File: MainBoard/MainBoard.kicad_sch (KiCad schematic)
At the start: 65 parts, among them J1 1761681-3, J2 Non-Inverting Input, J3 Inverting Input, J4 Output, J5 InvertedOutput, J6 Inverting Input, J7 Non-Inverting Input, J8 Output, J9 InvertedOutput, Q16 BC557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

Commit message: plot at tip output
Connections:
- net Comparator-1-InvertedOutput: now also D25.2 (A), D26.1 (K), Q16.3 (E), R1.2, R12.1; no longer J5.2, J5.3, R12.2
- net Comparator-2-InvertedOutput: now also D7.2 (A), D8.1 (K), Q32.3 (E), R13.1, R5.2; no longer J9.2, J9.3, R13.2
- net /Comparator-1/Output: now also D23.2 (A), D24.1 (K), D29.2 (A), Q16.2 (B), R11.1, R2.2; no longer J4.2, J4.3, R11.2
- net /Comparator-2/Output: now also D30.2 (A), Q32.2 (B), R14.1, R3.2; no longer J8.3, R14.2
- new net InvertedOutput-1: J5.2, J5.3, R12.2
- new net InvertedOutput-2: J9.2, J9.3, R13.2
- new net Output-1: J4.2, J4.3, R11.2
- new net Output-2: J8.3, R14.2
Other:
- note added: ".options method=gear gmin=1e-9 cshunt=1e-12 .options reltol=1e-2 abstol=1e-9 vntol=1e-6 .options itl1=300 itl4=300 .options maxstep=100p temp=60 .tran 100u 1000ms .control run plot V("/root/Comparator-1/NonInvertingInput") + V("/root/Comparator-1/InvertingInput") V("/root/Comparator-2/NonInvertingInput") + V("/Output-1") title "Comparator1 Output" plot V("/root/Comparator-1/NonInvertingInput") + 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"
- note removed: ".options method=gear gmin=1e-9 cshunt=1e-12 .options reltol=1e-2 abstol=1e-9 vntol=1e-6 .options itl1=300 itl4=300 .options maxstep=100p temp=60 .tran 100u 1000ms .control run plot V("/root/Comparator-1/NonInvertingInput") + V("/root/Comparator-1/InvertingInput") V("/root/Comparator-2/NonInvertingInput") + V("/root/Comparator-1/Output") title "Comparator1 Output" plot V("/root/Comparator-1/NonInv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"
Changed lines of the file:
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@@
 		)
 	)
-	(text ".options method=gear gmin=1e-9 cshunt=1e-12 \n.options reltol=1e-2 abstol=1e-9 vntol=1e-6 \n.options itl1=300 itl4=300 \n.options maxstep=100p temp=60\n.tran 100u 1000ms\n.control\nrun\nplot V(\"/root/Comparator-1/NonInvertingInput\") \n     + V(\"/root/Comparator-1/InvertingInput\") V(\"/root/Comparator-2/NonInvertingInput\") \n     + V(\"/root/Comparator-1/Output\") title \"Comparator1 Output\" \nplot V(\"/root/Comparator-1/NonInvertingInput\")\n     + V(\"/root/Comparator-1/InvertingInput\") V(\"/root/Comparator-2/NonInvertingInput\") \n     + V(\"/Comparator-1-InvertedOutput\") title \"Comparator1 Inverted-Output\"\nplot V(\"/root/Comparator-2/InvertingInput\") \n     + V(\"/root/Comparator-1/InvertingInput\") V(\"/root/Comparator-2/NonInvertingInput\")   \n     + V(\"/root/Comparator-2/Output\") title \"Comparator2 Output\" \nplot V(\"/root/Comparator-2/InvertingInput\")\n     + V(\"/root/Comparator-1/InvertingInput\") V(\"/root/Comparator-2/NonInvertingInput\") \n     + V(\"/Comparator-2-InvertedOutput\") title \"Comparator2 Inverted-Output\"\n.endc"
+	(text ".options method=gear gmin=1e-9 cshunt=1e-12 \n.options reltol=1e-2 abstol=1e-9 vntol=1e-6 \n.options itl1=300 itl4=300 \n.options maxstep=100p temp=60\n.tran 100u 1000ms\n.control\nrun\nplot V(\"/root/Comparator-1/NonInvertingInput\") \n     + V(\"/root/Comparator-1/InvertingInput\") V(\"/root/Comparator-2/NonInvertingInput\") \n     + V(\"/Output-1\") title \"Comparator1 Output\" \nplot V(\"/root/Comparator-1/NonInvertingInput\")\n     + V(\"/root/Comparator-1/InvertingInput\") V(\"/root/Comparator-2/NonInvertingInput\") \n     + V(\"/InvertedOutput-1\") title \"Comparator1 Inverted-Output\"\nplot V(\"/root/Comparator-2/InvertingInput\") \n     + V(\"/root/Comparator-1/InvertingInput\") V(\"/root/Comparator-2/NonInvertingInput\")   \n     + V(\"/Output-2\") title \"Comparator2 Output\" \nplot V(\"/root/Comparator-2/InvertingInput\")\n     + V(\"/root/Comparator-1/InvertingInput\") V(\"/root/Comparator-2/NonInvertingInput\") \n     + V(\"/InvertedOutput-2\") title \"Comparator2 Inverted-Output\"\n.endc"
 		(exclude_from_sim no)
 		(at 170.688 147.066 0)
@@
 	)
 	(junction
+		(at 250.19 88.9)
+		(diameter 0)
+		(color 0 0 0 0)
+	)
+	(junction
 		(at 49.53 29.21)
 		(diameter 0)
@@
 	)
 	(junction
-		(at 250.19 88.9)
-		(diameter 0)
-		(color 0 0 0 0)
-	)
-	(junction
 		(at 62.23 116.84)
 		(diameter 0)
@@
 	(wire
 		(pts
-			(xy 254 57.15) (xy 254 53.34)
-		)
-		(stroke
-			(width 0)
-			(type default)
-		)
-	)
-	(wire
-		(pts
-			(xy 250.19 33.02) (xy 250.19 29.21)
+			(xy 250.19 33.02) (xy 251.46 33.02)
+		)
+		(stroke
+			(width 0)
+			(type default)
+		)
+	)
+	(wire
+		(pts
+			(xy 254 113.03) (xy 254 116.84)
+		)
+		(stroke
+			(width 0)
+			(type default)
+		)
+	)
+	(wire
+		(pts
+			(xy 222.25 53.34) (xy 226.06 53.34)
+		)
+		(stroke
+			(width 0)
+			(type default)
+		)
+	)
+	(wire
+		(pts
+			(xy 213.36 29.21) (xy 217.17 29.21)
 		)
 		(stroke
@@
 	(wire
 		(pts
+			(xy 254 53.34) (xy 254 57.15)
+		)
+		(stroke
+			(width 0)
+			(type default)
+		)
+	)
+	(wire
+		(pts
 			(xy 96.52 173.99) (xy 96.52 175.26)
 		)
@@
 	(wire
 		(pts
-			(xy 254 116.84) (xy 254 113.03)
+			(xy 254 116.84) (xy 255.27 116.84)
+		)
+		(stroke
+			(width 0)
+			(type default)
+		)
+	)
+	(wire
+		(pts
+			(xy 223.52 113.03) (xy 227.33 113.03)
 		)
 		(stroke
@@
 	(wire
 		(pts
-			(xy 250.19 92.71) (xy 250.19 88.9)
+			(xy 213.36 88.9) (xy 217.17 88.9)
 		)
 		(stroke
@@
 	(wire
 		(pts
+			(xy 250.19 92.71) (xy 251.46 92.71)
+		)
+		(stroke
+			(width 0)
+			(type default)
+		)
+	)
+	(wire
+		(pts
 			(xy 67.31 100.33) (xy 67.31 101.6)
 		)
@@
 	(wire
 		(pts
+			(xy 254 57.15) (xy 255.27 57.15)
+		)
+		(stroke
+			(width 0)
+			(type default)
+		)
+	)
+	(wire
+		(pts
 			(xy 62.23 125.73) (xy 62.23 127)
 		)
@@
 	(wire
 		(pts
+			(xy 250.19 88.9) (xy 250.19 92.71)
+		)
+		(stroke
+			(width 0)
+			(type default)
+		)
+	)
+	(wire
+		(pts
 			(xy 59.69 165.1) (xy 63.5 165.1)
 		)
@@
 	(wire
 		(pts
+			(xy 250.19 29.21) (xy 250.19 33.02)
+		)
+		(stroke
+			(width 0)
+			(type default)
+		)
+	)
+	(wire
+		(pts
 			(xy 44.45 134.62) (xy 31.75 134.62)
 		)
@@
 		)
 	)
+	(label "Output-2"
+		(at 251.46 92.71 0)
+		(effects
+			(font
+				(size 1.27 1.27)
+			)
+			(justify left bottom)
+		)
+	)
+	(label "Output-1"
+		(at 251.46 33.02 0)
+		(effects
+			(font
+				(size 1.27 1.27)
+			)
+			(justify left bottom)
+		)
+	)
 	(label "Comparator-2-InvertedOutput"
-		(at 254 116.84 0)
-		(effects
-			(font
-				(size 1.27 1.27)
-			)
-			(justify left bottom)
+		(at 223.52 113.03 180)
+		(effects
+			(font
+				(size 1.27 1.27)
+			)
+			(justify right bottom)
 		)
 	)
@@
 	)
 	(label "{slash}Comparator-2{slash}Output"
-		(at 250.19 92.71 0)
+		(at 213.36 88.9 180)
 		(fields_autoplaced yes)
 		(effects
@@
 				(size 1.27 1.27)
 			)
-			(justify left bottom)
+			(justify right bottom)
 		)
 		(property "Netclass" ""
-			(at 250.19 93.98 0)
+			(at 213.36 90.17 0)
 			(effects
 				(font
@@
 					(italic yes)
 				)
-				(justify left)
+				(justify right)
 			)
 		)
@@
 	)
 	(label "Comparator-1-InvertedOutput"
-		(at 254 57.15 0)
-		(effects
-			(font
-				(size 1.27 1.27)
-			)
-			(justify left bottom)
+		(at 222.25 53.34 180)
+		(effects
+			(font
+				(size 1.27 1.27)
+			)
+			(justify right bottom)
 		)
 	)
 	(label "{slash}Comparator-1{slash}Output"
-		(at 250.19 33.02 0)
-		(effects
-			(font
-				(size 1.27 1.27)
-			)
-			(justify left bottom)
+		(at 213.36 29.21 180)
+		(effects
+			(font
+				(size 1.27 1.27)
+			)
+			(justify right bottom)
 		)
 	)
@@
 		)
 	)
+	(label "InvertedOutput-1"
+		(at 255.27 57.15 0)
+		(effects
+			(font
+				(size 1.27 1.27)
+			)
+			(justify left bottom)
+		)
+	)
+	(label "InvertedOutput-2"
+		(at 255.27 116.84 0)
+		(effects
+			(font
+				(size 1.27 1.27)
+			)
+			(justify left bottom)
+		)
+	)

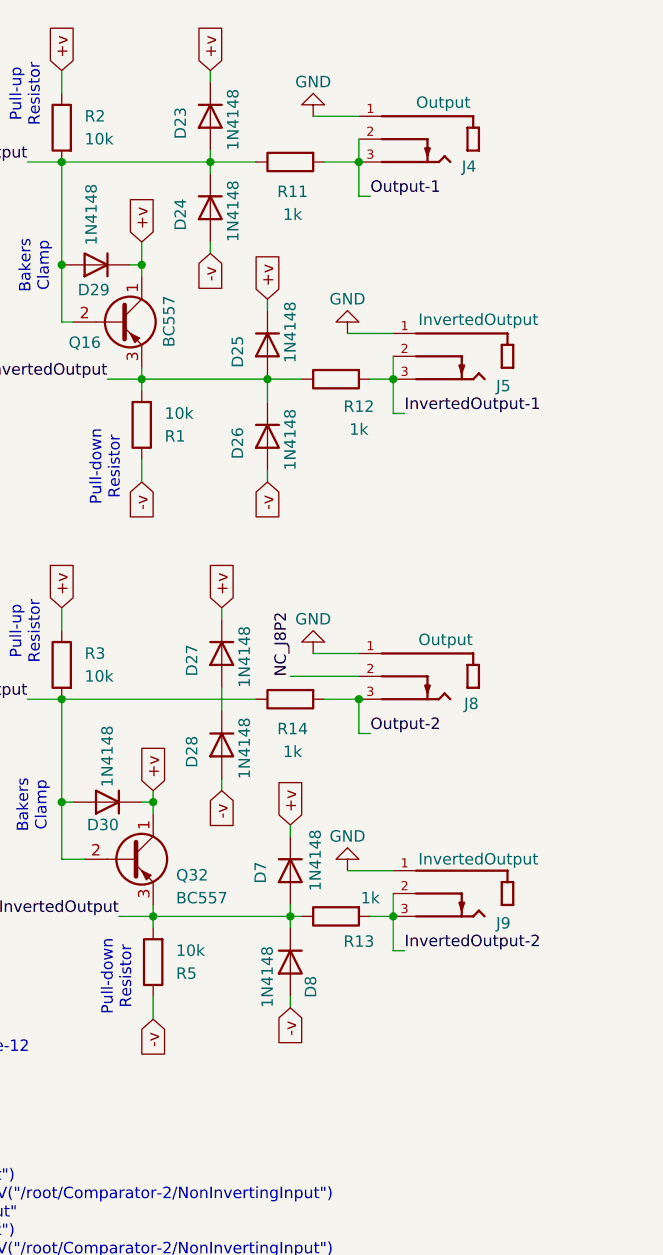
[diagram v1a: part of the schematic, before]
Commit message: added bi-directional LEDs on each output
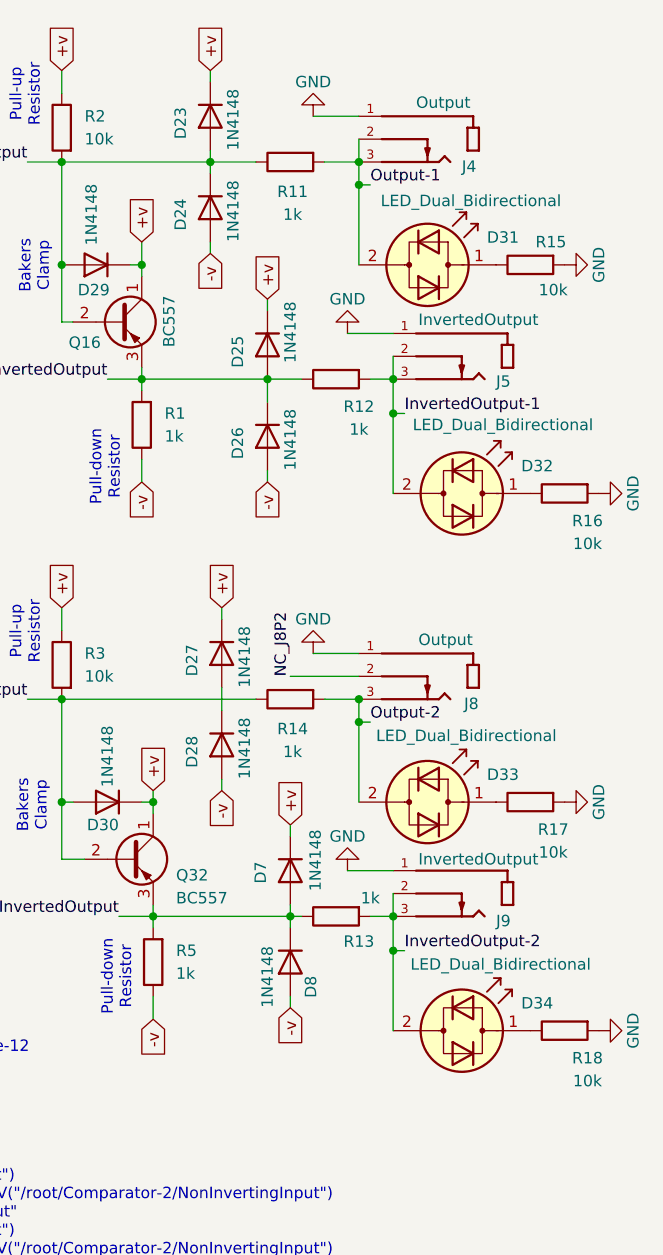
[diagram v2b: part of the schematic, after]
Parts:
- added D31, D32, D33, D34: LED_Dual_Bidirectional, symbol Device:LED_Dual_Bidirectional
- added R15, R16, R17, R18: 10k, Resistor_THT:R_Axial_DIN0207_L6.3mm_D2.5mm_P7.62mm_Horizontal, symbol Device:R
- R1, R5: value 10k -> 1k
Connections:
- net GND: now also R15.2, R16.2, R17.2, R18.2
- net InvertedOutput-1: now also D32.2 (AK)
- net InvertedOutput-2: now also D34.2 (AK)
- net Output-1: now also D31.2 (AK)
- net Output-2: now also D33.2 (AK)
- new net: D31.1 (KA), R15.1
- new net: D34.1 (KA), R18.1
- new net: D33.1 (KA), R17.1
- new net: D32.1 (KA), R16.1

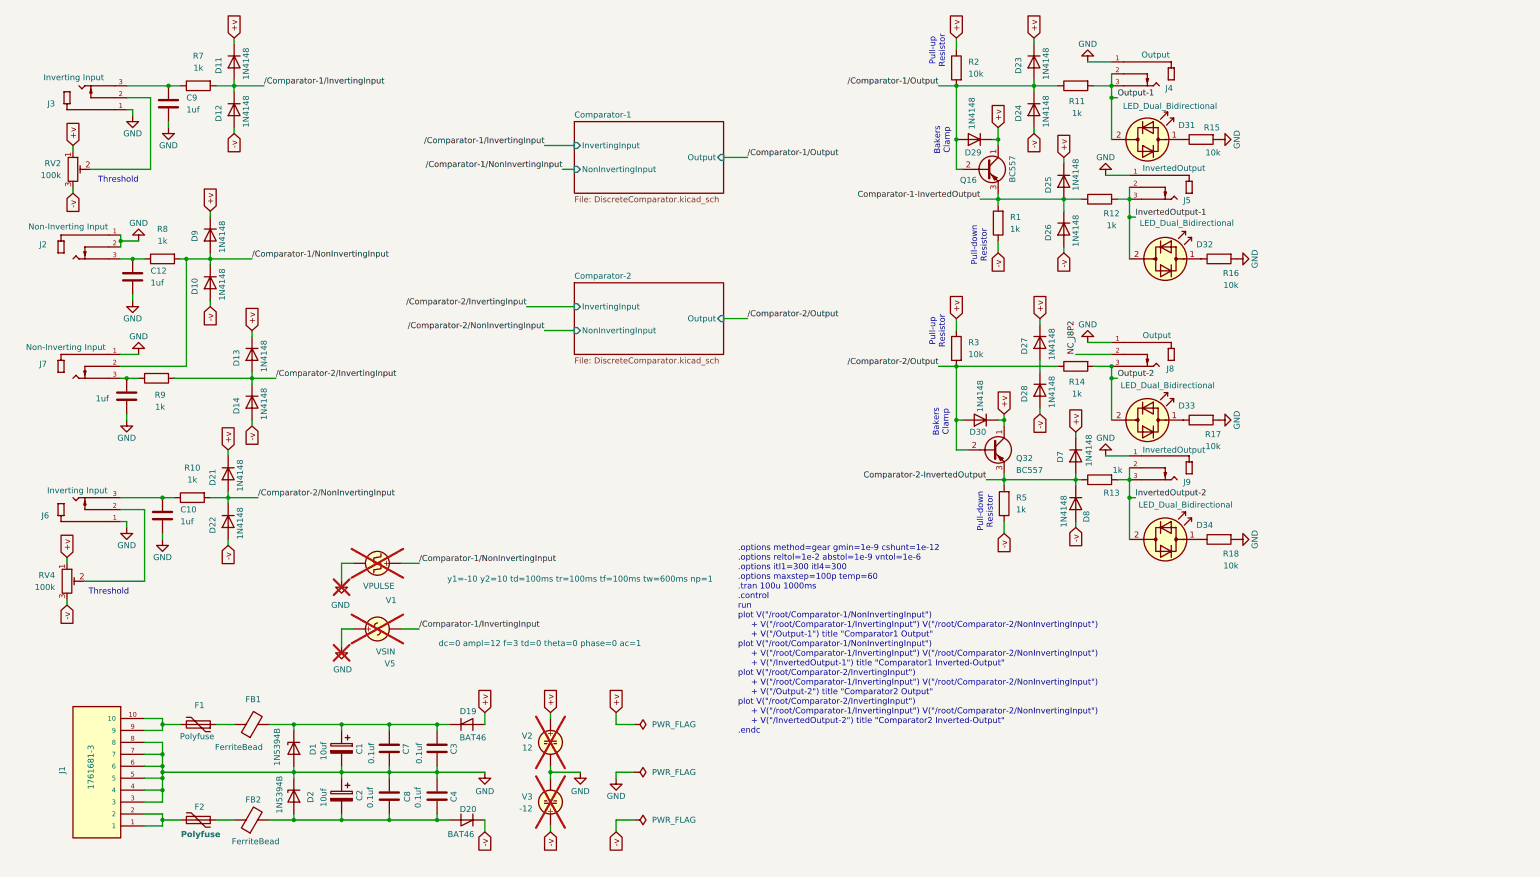
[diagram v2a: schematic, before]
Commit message: refactored power supply
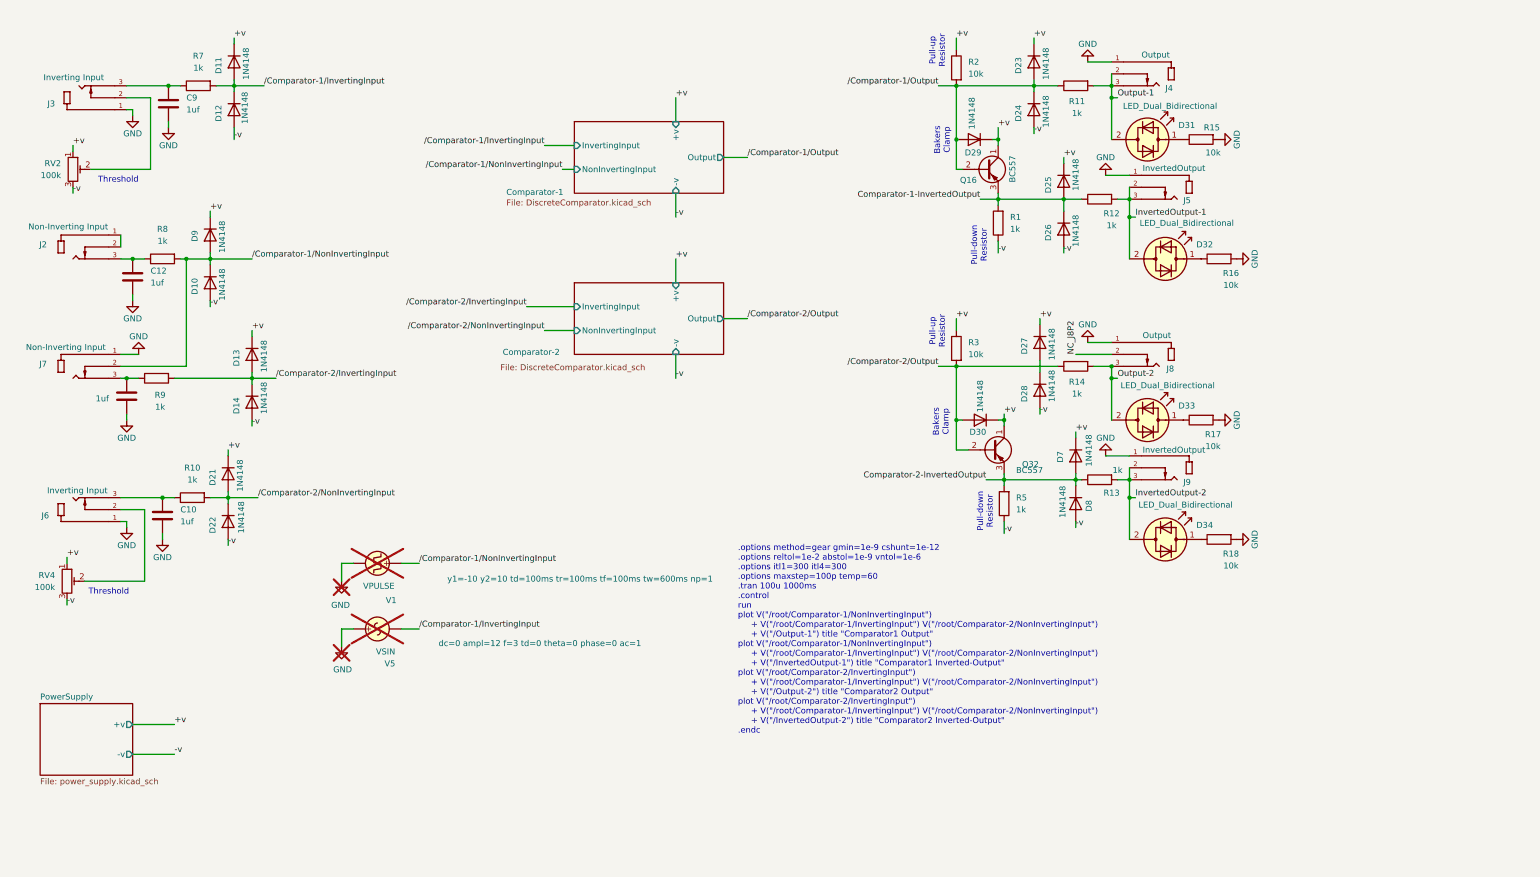
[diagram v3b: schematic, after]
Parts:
- removed C1, C2: 10uf, Capacitor_THT:CP_Radial_D10.0mm_P2.50mm, symbol Device:C_Polarized
- removed C3, C4, C7, C8: 0.1uf, Capacitor_THT:C_Disc_D5.0mm_W2.5mm_P2.50mm, symbol Device:C
- removed D1, D2: 1N5394B, Diode_THT:D_DO-35_SOD27_P7.62mm_Horizontal, symbol Diode:1N53xxB
- removed D19, D20: BAT46, symbol Device:D_Shockley
- removed F1, F2: Polyfuse, 72R020XU:FUSRB510W81L1358T310H1980, symbol Device:Polyfuse
- removed FB1, FB2: FerriteBead, symbol Device:FerriteBead
- removed J1: 1761681-3, 1761681-3:TE_1761681-3, symbol 1761681-3:1761681-3
- removed V2: 12, symbol Simulation_SPICE:VDC
- removed V3: -12, symbol Simulation_SPICE:VDC
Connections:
- net GND: no longer J2.1, J2.2
- new net: J2.1, J2.2
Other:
- added sheet PowerSupply (power_supply.kicad_sch)
- sheet Comparator-1 ports: added +v, -v; removed none
- sheet Comparator-2 ports: added +v, -v; removed none
